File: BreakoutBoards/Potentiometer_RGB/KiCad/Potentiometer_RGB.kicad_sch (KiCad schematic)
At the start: 6 parts, among them J1 Conn_01x06_Pin

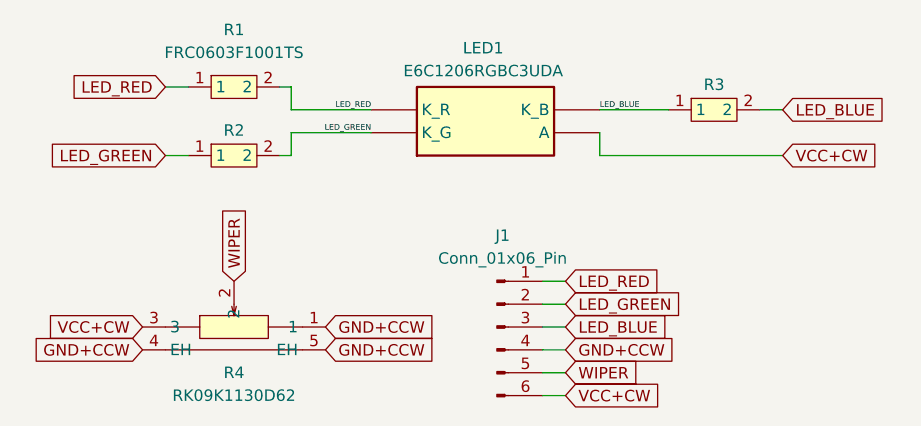
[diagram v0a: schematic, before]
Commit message: removing resistors to make more versatile and selecting new led to use
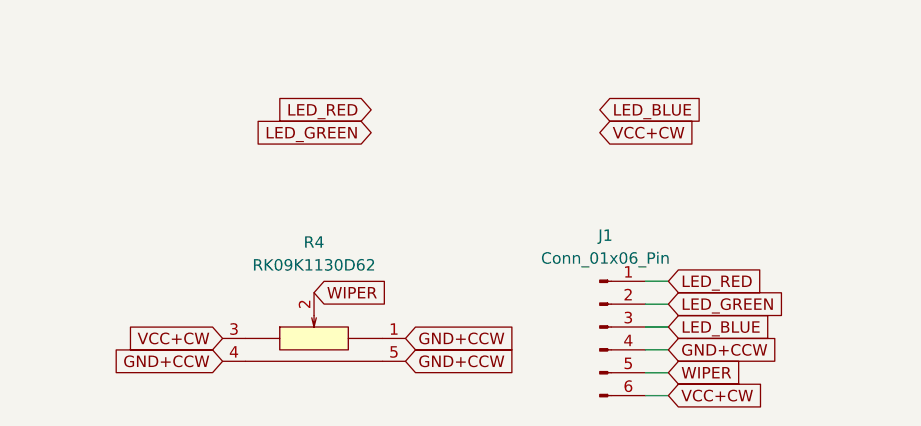
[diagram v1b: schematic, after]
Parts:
- removed LED1: E6C1206RGBC3UDA, clectric-diy:E6C1206RGBC3UDA, symbol clectric-diy:E6C1206RGBC3UDA
- removed R1, R2, R3: FRC0603F1001TS, clectric-diy:R0603, symbol clectric-diy:FRC0603F1001TS
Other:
- moved on the sheet: J1
